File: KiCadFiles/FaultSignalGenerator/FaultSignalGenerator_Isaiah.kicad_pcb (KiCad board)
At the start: 2 copper layers, 17 parts, among them J1 Conn_02x20_Counter_Clockwise, U1 TL074CDR, U2 MCP4462-502E/ST, U3 PCM1681PWP

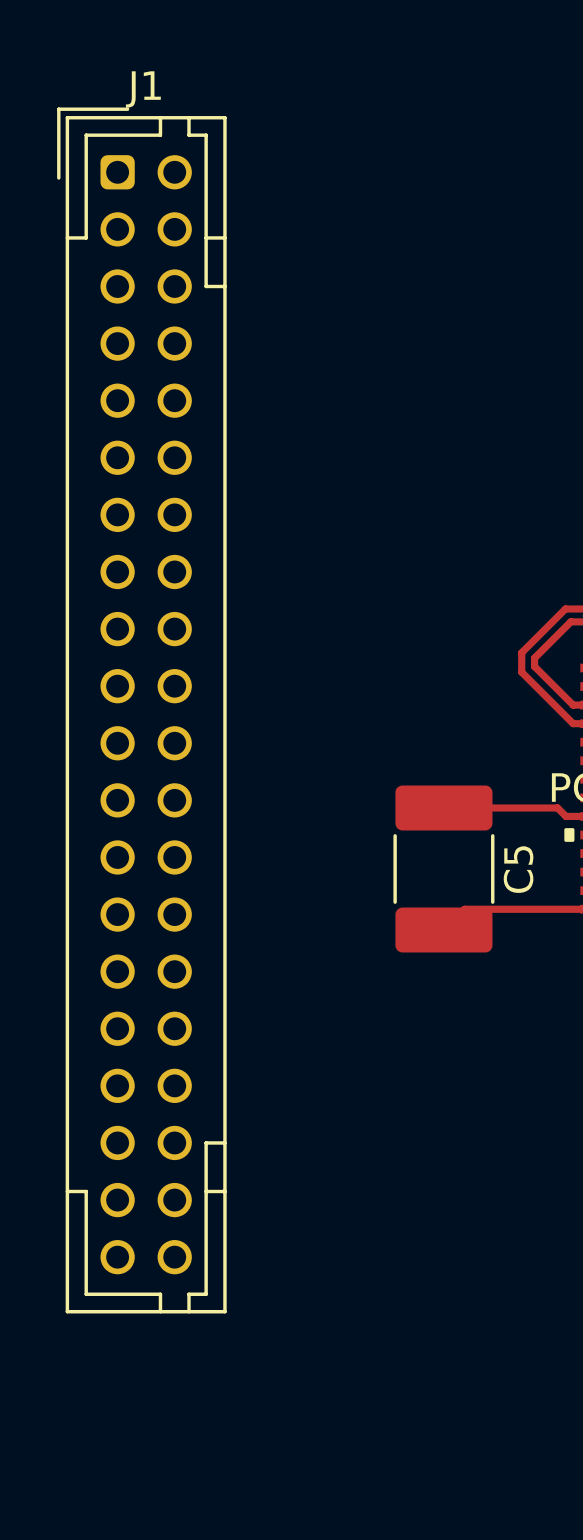
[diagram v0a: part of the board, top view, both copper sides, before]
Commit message: 16 Channel Schema Push
Have a 16 channel schema implemented. Will need to define I/O.
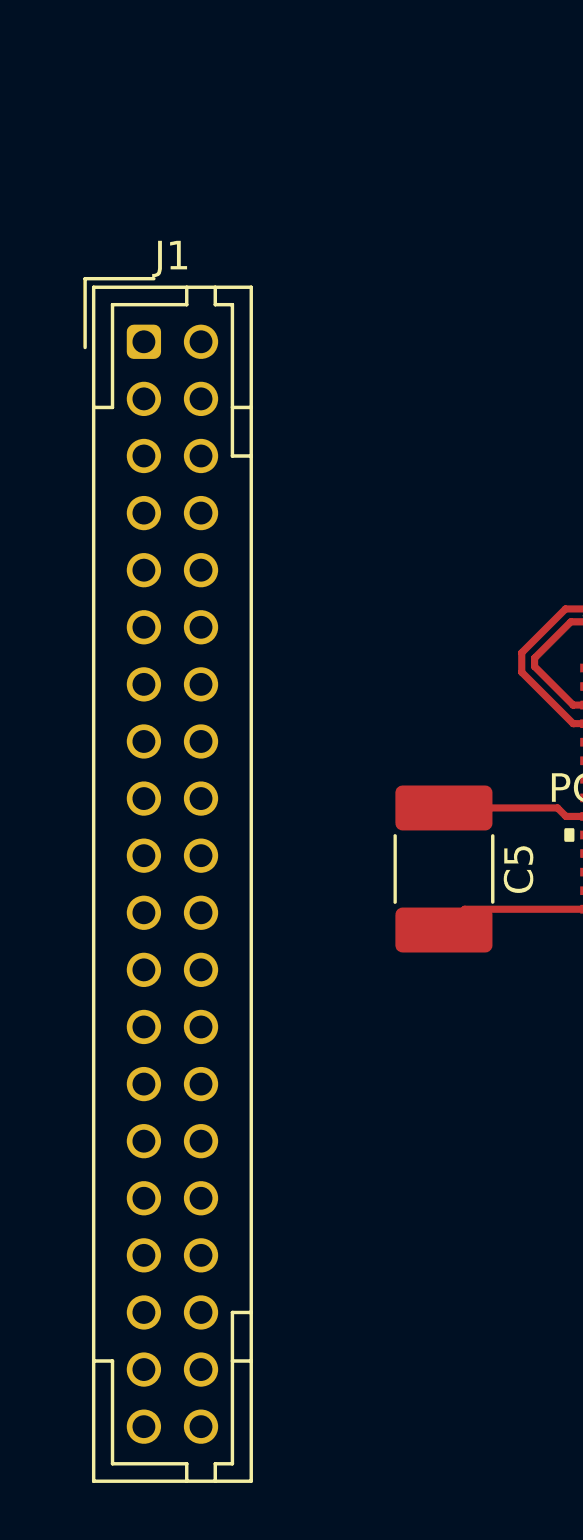
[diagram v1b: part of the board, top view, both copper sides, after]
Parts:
- moved J1 6.01 mm to (49.1, 73.4)
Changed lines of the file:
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@@
   )
   (footprint "Connector_JAE:JAE_LY20-40P-DT1_2x20_P2.00mm_Vertical" (layer "F.Cu")
-    (at 48.133 67.439)
+    (at 49.054 73.376)
     (descr "Molex LY 20 series connector, LY20-40P-DT1, 20 Circuits (http://www.jae.com/z-en/pdf_download_exec.cfm?param=SJ103130.pdf), generated with kicad-footprint-generator")
     (tags "connector JAE  side entry")
@@
     )
   )
+  (dimension (type aligned) (layer "F.Cu")
+    (pts (xy 47.117 70.485) (xy 47.117 113.284))
+    (height 7.492999)
+    (gr_text "42.7990 mm" (at 37.824001 91.8845 90) (layer "F.Cu")
+      (effects (font (size 1.5 1.5) (thickness 0.3)))
+    )
+    (format (units 3) (units_format 1) (precision 4))
+    (style (thickness 0.2) (arrow_length 1.27) (text_position_mode 0) (extension_height 0.58642) (extension_offset 0.5) keep_text_aligned)
+  )
+  (dimension (type aligned) (layer "F.Cu")
+    (pts (xy 47.752 71.501) (xy 114.3 71.501))
+    (height -2.794)
+    (gr_text "66.5480 mm" (at 81.026 66.907) (layer "F.Cu")
+      (effects (font (size 1.5 1.5) (thickness 0.3)))
+    )
+    (format (units 3) (units_format 1) (precision 4))
+    (style (thickness 0.2) (arrow_length 1.27) (text_position_mode 0) (extension_height 0.58642) (extension_offset 0.5) keep_text_aligned)
+  )
   (segment (start 89.662 89.789) (end 96.1155 96.2425) (width 0.25) (layer "F.Cu") (net 1))
